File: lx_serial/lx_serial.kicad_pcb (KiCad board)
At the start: 4 copper layers, 44.3 x 11 mm, 23 parts, among them J1 200LX_02X05, P1 USB_OTG, U1 FT231XS, U2 TRS3243E

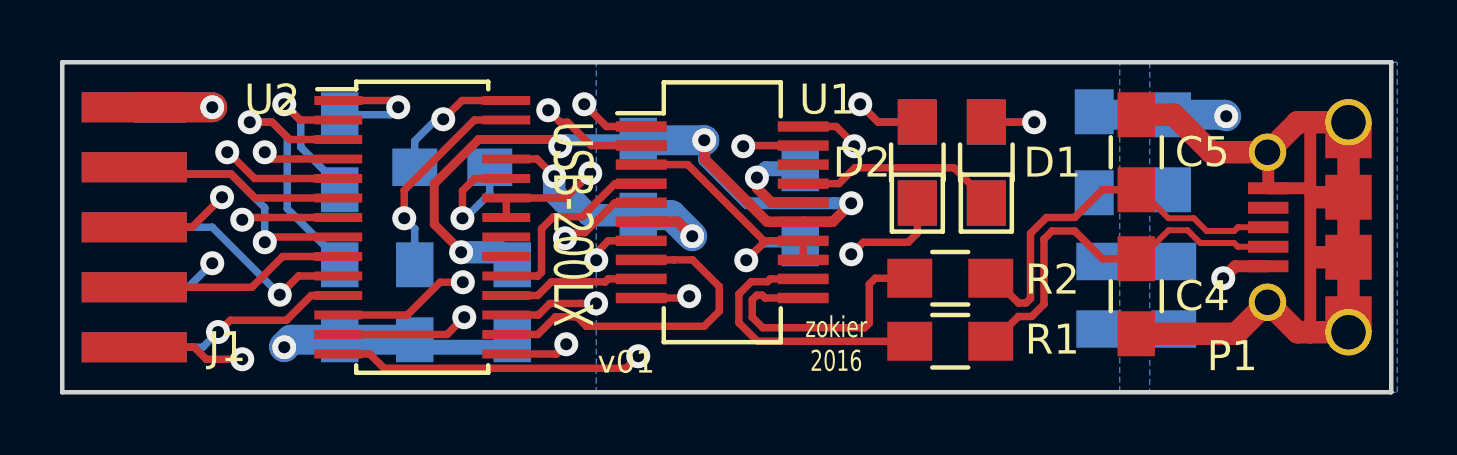
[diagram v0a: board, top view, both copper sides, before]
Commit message: disconnected usb shield from gnd
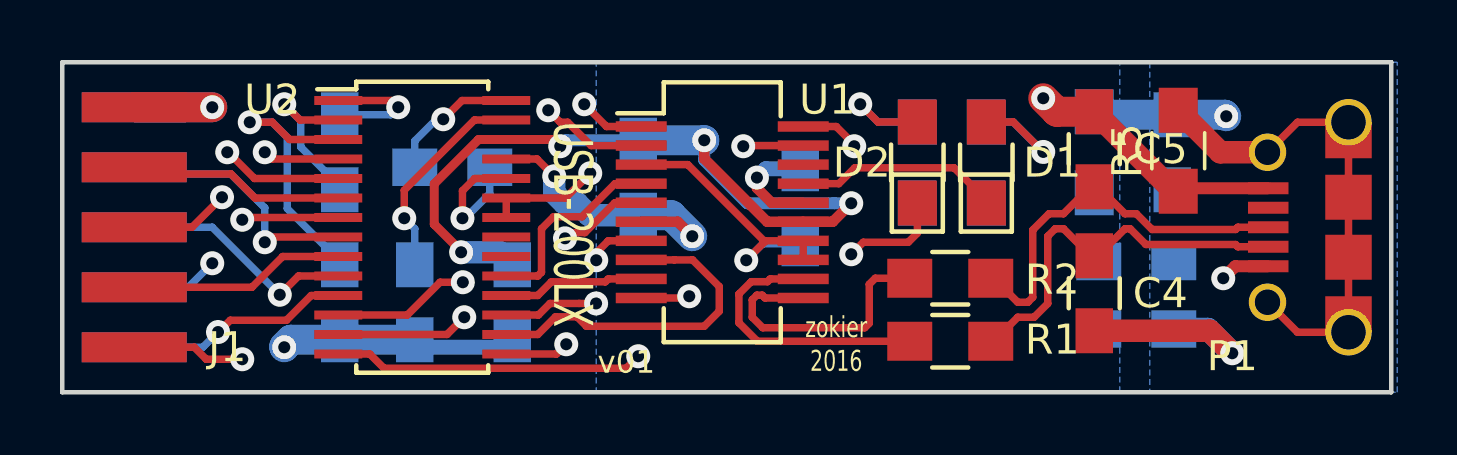
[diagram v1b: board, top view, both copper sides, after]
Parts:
- added R5: 0R, Resistors_SMD:R_0805_HandSoldering, F.Cu at (58.2, 34.0)
- moved C5 1.40 mm to (55.4, 33.9)
- moved C4 1.40 mm to (55.4, 38.7)
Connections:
- P1 pad 6: GND -> Net-(P1-Pad6)
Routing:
- net GND: track 60.1 -> 42.6 mm, vias 5 -> 7
- net Net-(P1-Pad6): track 0.00 -> 16.8 mm
- net Net-(D1-Pad2): track 3.20 -> 4.62 mm

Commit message: silkscreen tweaks
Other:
- board text added: "zokier 2018"
- board text removed: "zokier 2016"
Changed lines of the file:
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@@
     (tags "capacitor 0805")
     (attr smd)
-    (fp_text reference C5 (at 0 2.2 180) (layer F.SilkS)
+    (fp_text reference C5 (at 1.3 -1.7 180) (layer F.SilkS)
       (effects (font (size 1 1) (thickness 0.15)))
     )
@@
     (tags "LED  0805")
     (attr smd)
-    (fp_text reference D1 (at -0.006717 2.196725 180) (layer F.SilkS)
+    (fp_text reference D1 (at -0.856717 1.896725 180) (layer F.SilkS)
       (effects (font (size 1 1) (thickness 0.15)))
     )
@@
     (tags "resistor 0805")
     (attr smd)
-    (fp_text reference R1 (at 3.4 -0.05) (layer F.SilkS)
+    (fp_text reference R1 (at 3.1 0.2) (layer F.SilkS)
       (effects (font (size 1 1) (thickness 0.15)))
     )
@@
     (tags "resistor 0805")
     (attr smd)
-    (fp_text reference R2 (at 3.4 0.05) (layer F.SilkS)
+    (fp_text reference R2 (at 3.1 -0.9) (layer F.SilkS)
       (effects (font (size 1 1) (thickness 0.15)))
     )
@@
   (module ssop_20:MICRO_USB_B_TYPE_RECEPTABLE_CIRCLES (layer F.Cu)
     (at 65.325 36.5 90)
-    (fp_text reference P1 (at -4.3 -5.325 360) (layer F.SilkS)
+    (fp_text reference P1 (at -4.3 -3.825 360) (layer F.SilkS)
       (effects (font (size 1 1) (thickness 0.15)))
     )
@@
     (tags "resistor 0805")
     (attr smd)
-    (fp_text reference R5 (at 0 -1.7 90) (layer F.SilkS)
+    (fp_text reference R5 (at 1.55 1.8 180) (layer F.SilkS)
       (effects (font (size 1 1) (thickness 0.15)))
     )
@@
     (arrow2b (pts (xy 21 28) (xy 22.126504 27.413579)))
   )
-  (gr_text "zokier\n2016" (at 46.8 40.4) (layer F.SilkS)
+  (gr_text "zokier\n2018" (at 46.8 40.4) (layer F.SilkS)
     (effects (font (size 0.7 0.5) (thickness 0.125)))
   )
